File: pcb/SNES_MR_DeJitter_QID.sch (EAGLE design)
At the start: 92 parts, among them J1 SNESCART_CONN_SPARSE_4, U1 SuperCIC_lock, U2 uIGR, U3 EPM7032AETC44-10N, U4 74HCT2G125DP, U5 CDCE913, U6 2G17TI_DBV, U7 TLV70033, U8 TLV70018, U9 TSH122ICT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

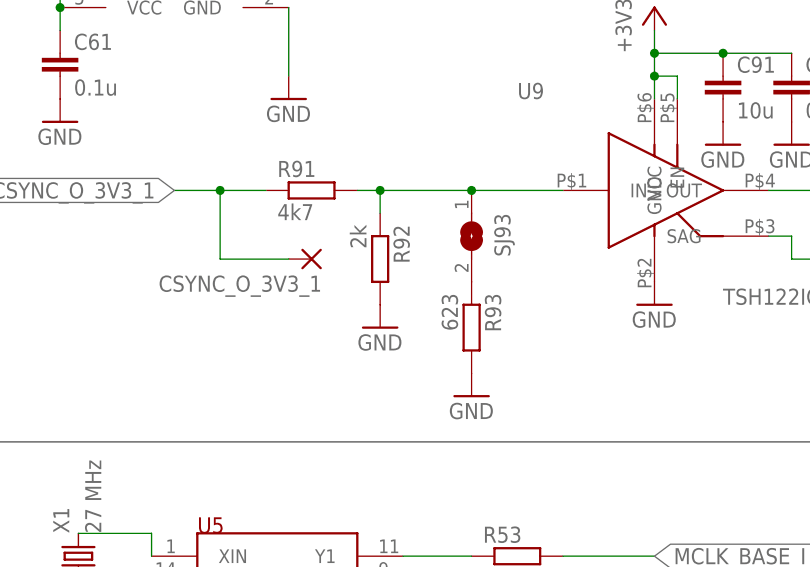
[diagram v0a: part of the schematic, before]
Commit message: resolve inconsistency between schematic and BOM
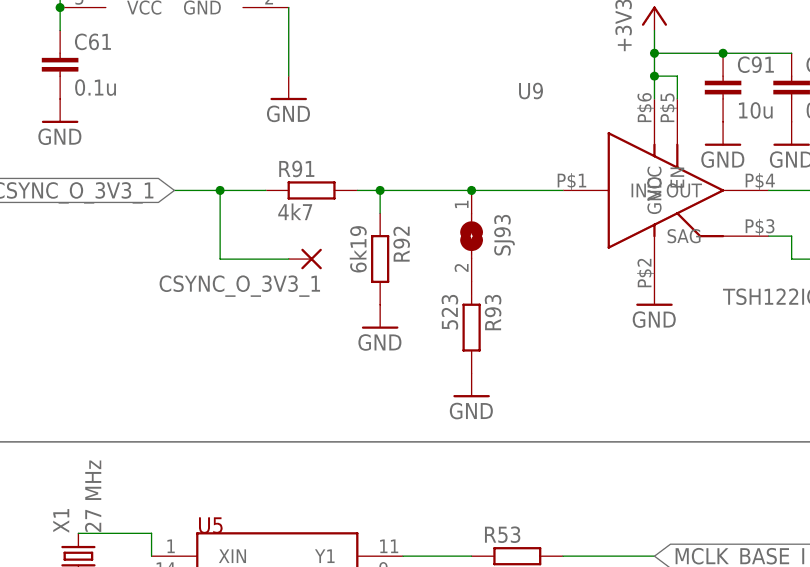
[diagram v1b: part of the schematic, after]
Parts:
- R92: value 2k -> 6k19
- R93: value 623 -> 523
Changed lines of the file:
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@@
 <?xml version="1.0" encoding="utf-8"?>
 <!DOCTYPE eagle SYSTEM "eagle.dtd">
-<eagle version="9.5.2">
+<eagle version="9.6.2">
 <drawing>
 <settings>
@@
 <part name="SJ62" library="jumper" deviceset="SJ" device="SMALL"/>
 <part name="CSYNC_I1" library="wirepad" deviceset="SMD2" device=""/>
-<part name="R92" library="rcl" deviceset="R-EU_" device="R0603" value="2k"/>
+<part name="R92" library="rcl" deviceset="R-EU_" device="R0603" value="6k19"/>
 <part name="R91" library="rcl" deviceset="R-EU_" device="R0603" value="4k7"/>
 <part name="R94" library="rcl" deviceset="R-EU_" device="R0603" value="75"/>
@@
 <part name="C92" library="rcl" deviceset="C-EU" device="C0603" value="0.01u"/>
 <part name="SJ93" library="jumper" deviceset="SJ" device="SMALL"/>
-<part name="R93" library="rcl" deviceset="R-EU_" device="R0603" value="623"/>
+<part name="R93" library="rcl" deviceset="R-EU_" device="R0603" value="523"/>
 <part name="GND27" library="supply1" library_urn="urn:adsk.eagle:library:371" deviceset="GND" device=""/>
 <part name="SJ63A" library="jumper" deviceset="SJ" device="SMALL"/>
